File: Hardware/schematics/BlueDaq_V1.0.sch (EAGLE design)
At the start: 67 parts, among them IC1 MEGA8-AI, Q1 MMBT2222, Q2 MMBT2222, Q3 MMBT2222, Q4 MMBT2222, U1 MCP73831, U2 TPS61200, U3 BME280, U4 MIC5225-3.3, U5 MIC5219 5V, X1 USB-MICROB, X2 3.5mm, X4 3.5mm, Y1 16 mhz

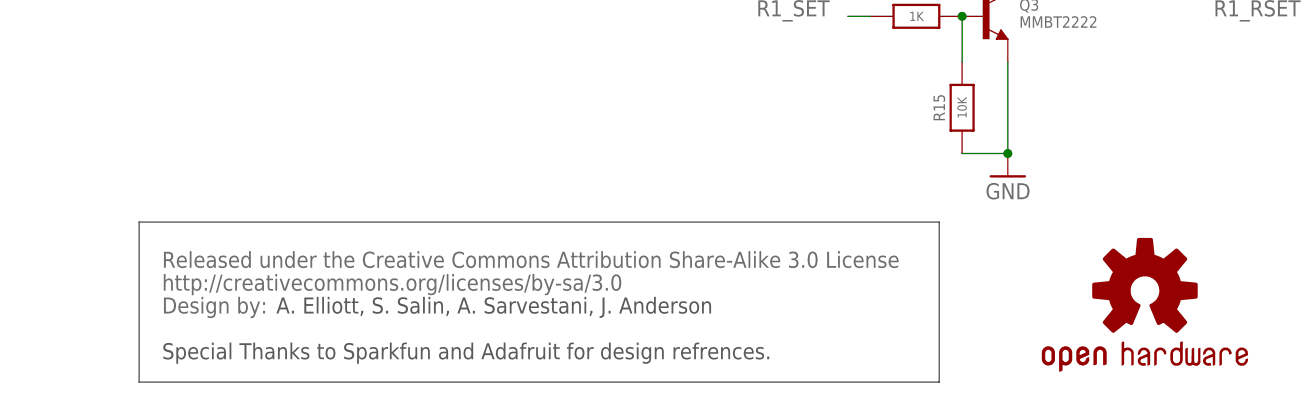
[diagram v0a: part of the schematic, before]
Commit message: moved some stuff to other side of board
starting to make big things on top small stuff on bottom for oven
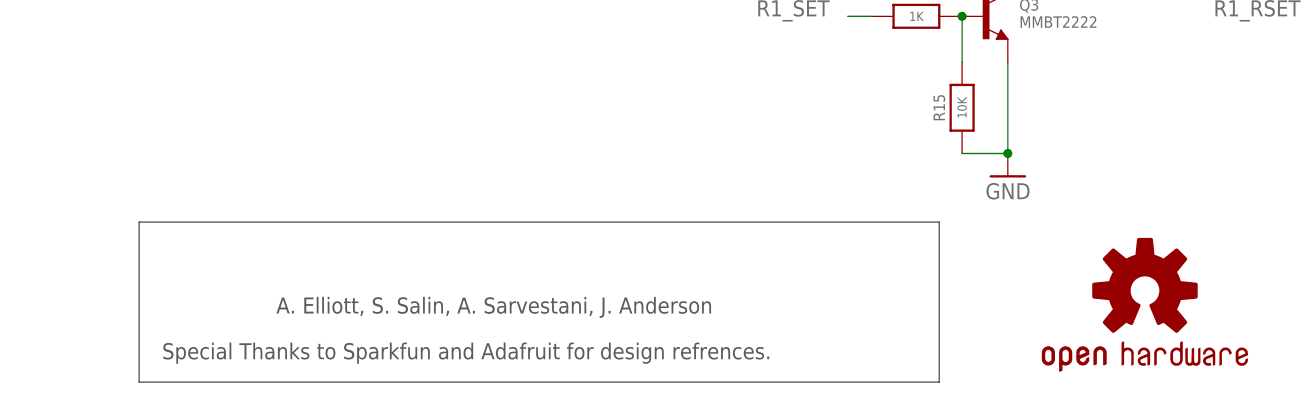
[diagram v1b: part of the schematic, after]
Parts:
- removed U$23: CREATIVE_COMMONS, SparkFun-Aesthetics:CREATIVE_COMMONS
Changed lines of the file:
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@@
 <part name="U$21" library="microbuilder" deviceset="GND" device=""/>
 <part name="U$22" library="SparkFun" deviceset="OSHW-LOGO" device="S"/>
-<part name="U$23" library="SparkFun-Aesthetics" deviceset="CREATIVE_COMMONS" device=""/>
 </parts>
 <sheets>
@@
 <instance part="U$21" gate="G$1" x="81.28" y="218.44"/>
 <instance part="U$22" gate="G$1" x="302.26" y="15.24"/>
-<instance part="U$23" gate="G$1" x="193.04" y="12.7"/>
 </instances>
 <busses>

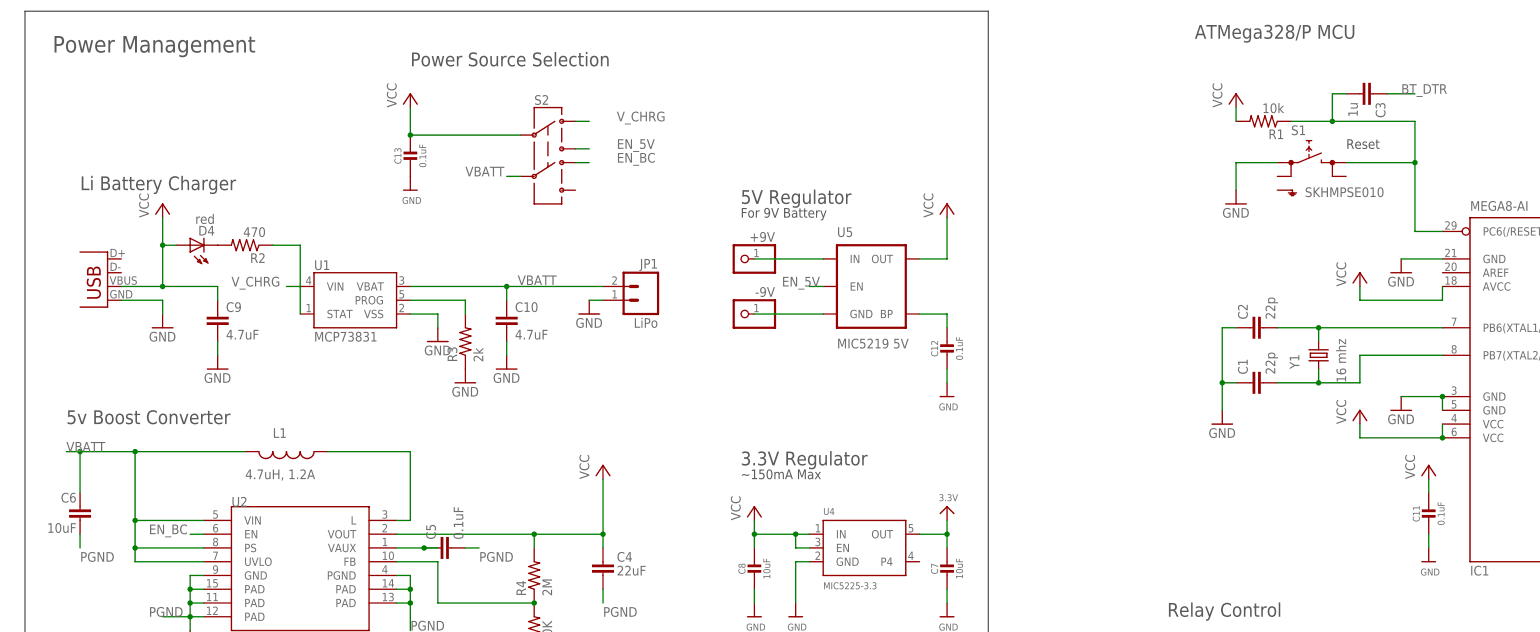
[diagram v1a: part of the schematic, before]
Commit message: updated board
updated layout. starting to have issue connecting gnd properly. added DRU/cam processor for OSH
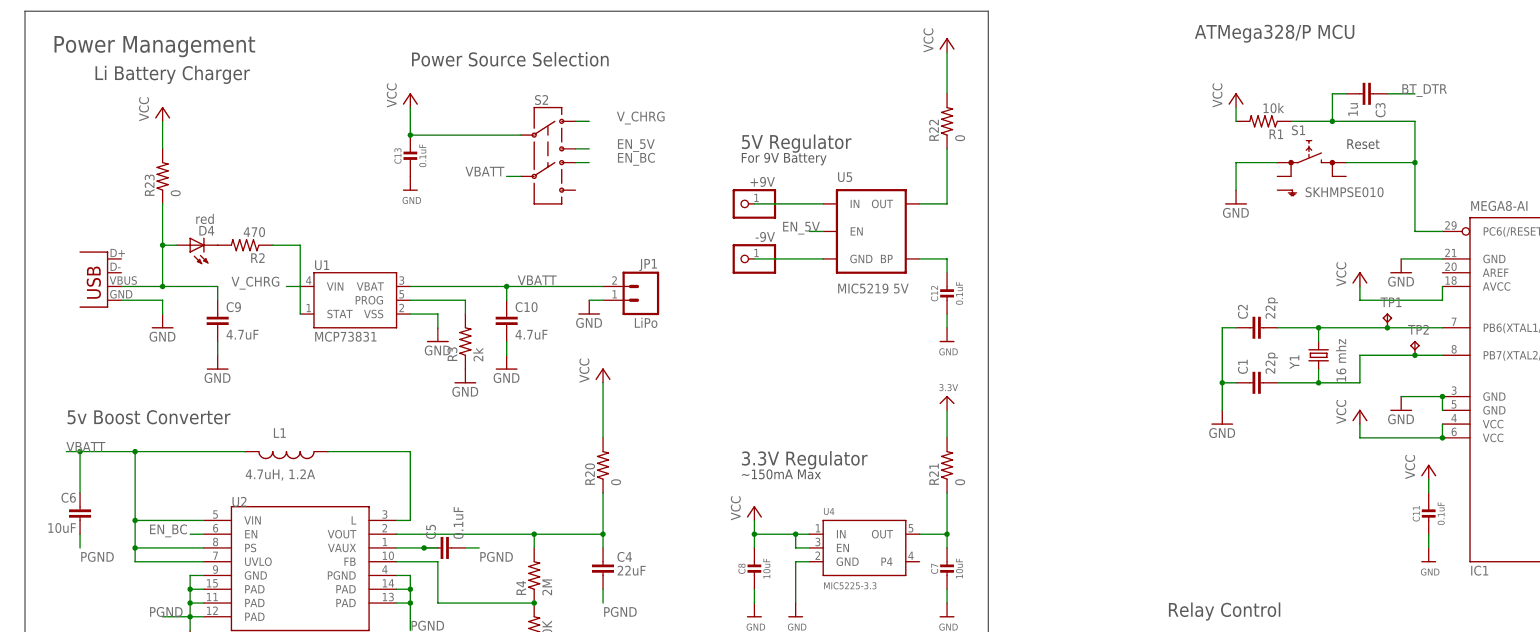
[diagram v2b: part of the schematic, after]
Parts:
- added R20, R21, R22, R23: 0, adafruit:R-US_R0805
- added TP1, TP2: TPTP19SQ, testpad:TPTP19SQ
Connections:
- new net N$20: C4.1, R20.1, R4.2, U2.VOUT
- new net N$21: R22.1, U5.OUT
- new net N$23: C9.1, D4.A, R23.1, X1.VBUS
- new net OUT: C7.1, R21.1, U4.OUT
- net 3.3V: now also R21.2; no longer C7.1, U4.OUT
- net VCC: now also R20.2, R22.2, R23.2; no longer C4.1, C9.1, D4.A, R4.2, U2.VOUT, U5.OUT, X1.VBUS
- net XTAL1: now also TP1.TP
- net XTAL2: now also TP2.TP
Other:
- moved on the sheet: +9V, -9V, C12, U5

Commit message: + Updated Schematic
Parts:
- removed BLUETOOTH: (no value), pinhead:PINHD-1X7
- removed C3: 1u, rcl:C-EUC0603
- removed R6: 10K, adafruit:R-US_R0805
- added C14: 0.1uF, microbuilder:CAP_CERAMIC0805-NOOUTLINE
- added JP2: (no value), adafruit:PINHD-1X6
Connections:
- removed net BT_DSR: BLUETOOTH.3, IC1.PD2(INT0)
- removed net BT_DTR: BLUETOOTH.7, C3.1
- removed net N$5: R6.2, U3.SDO
- new net BT_BRK: IC1.PD2(INT0), JP2.1
- net 3.3V: no longer R6.1
- net BT_RX: now also JP2.2; no longer BLUETOOTH.6
- net BT_STS: now also JP2.5, JP2.6; no longer BLUETOOTH.1
- net BT_TX: now also JP2.3; no longer BLUETOOTH.5
- net GND: now also C11.1, C14.1, JP2.4, U3.SDO; no longer BLUETOOTH.2, C11.2
- net RESET_PIN: no longer C3.2
- net VCC: now also C11.2, C14.2; no longer BLUETOOTH.4, C11.1
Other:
- moved on the sheet: C11

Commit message: + orginization chages
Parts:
- removed JP2: (no value), adafruit:PINHD-1X6
- added BT: (no value), adafruit:PINHD-1X6
- added D8: (no value), adafruit:DIODESMA
- C12: value 0.1uF -> 10uF
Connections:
- removed net N$21: R22.1, U5.OUT
- new net N$18: D8.C, R22.1
- new net N$5: D8.A, U5.OUT
- net BT_BRK: now also BT.1; no longer JP2.1
- net BT_RX: now also BT.2; no longer JP2.2
- net BT_STS: now also BT.6; no longer JP2.5, JP2.6
- net BT_TX: now also BT.3; no longer JP2.3
- net GND: now also BT.4, C4.2, C5.2, C6.2, R5.1, U2.PAD@4, U2.PAD@5, U2.PGND; no longer JP2.4
- net PGND: no longer C4.2, C5.2, C6.2, R5.1, U2.PAD@4, U2.PAD@5, U2.PGND
- net VCC: now also BT.5
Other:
- moved on the sheet: C11, C14, R1, R22

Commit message: Add files via upload
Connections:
- net N$20 renamed VOUT
- removed net PGND: U2.GND, U2.PAD@1, U2.PAD@2, U2.PAD@3
- net GND: now also U2.GND, U2.PAD@1, U2.PAD@2, U2.PAD@3
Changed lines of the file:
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@@
 <?xml version="1.0" encoding="utf-8"?>
 <!DOCTYPE eagle SYSTEM "eagle.dtd">
-<eagle version="7.7.0">
+<eagle version="7.6.0">
 <drawing>
 <settings>
@@
 <layer number="91" name="Nets" color="2" fill="1" visible="yes" active="yes"/>
 <layer number="92" name="Busses" color="1" fill="1" visible="yes" active="yes"/>
-<layer number="93" name="Pins" color="2" fill="1" visible="yes" active="yes"/>
+<layer number="93" name="Pins" color="2" fill="1" visible="no" active="yes"/>
 <layer number="94" name="Symbols" color="4" fill="1" visible="yes" active="yes"/>
 <layer number="95" name="Names" color="7" fill="1" visible="yes" active="yes"/>
@@
 <part name="C5" library="SparkFun" deviceset="CAP" device="0402-CAP" value="0.1uF"/>
 <part name="C6" library="CH_passive" deviceset="CAP" device="1206" value="10uF"/>
-<part name="GND4" library="SparkFun" deviceset="GND" device=""/>
 <part name="L1" library="SparkFun" deviceset="INDUCTOR" device="." value="4.7uH, 1.2A"/>
 <part name="P+5" library="supply1" deviceset="VCC" device=""/>
@@
 <part name="GND21" library="SparkFun" deviceset="GND" device=""/>
 <part name="D8" library="adafruit" deviceset="DIODE" device="SMA"/>
+<part name="GND4" library="SparkFun" deviceset="GND" device=""/>
 </parts>
 <sheets>
@@
 <attribute name="VALUE" x="14.224" y="155.194" size="1.778" layer="96"/>
 </instance>
-<instance part="GND4" gate="1" x="40.64" y="134.62"/>
 <instance part="L1" gate="G$1" x="58.42" y="170.18" smashed="yes" rot="R270">
 <attribute name="NAME" x="55.88" y="172.72" size="1.778" layer="95"/>
@@
 <instance part="GND21" gate="1" x="20.32" y="152.4"/>
 <instance part="D8" gate="G$1" x="180.34" y="223.52" rot="R90"/>
+<instance part="GND4" gate="1" x="40.64" y="134.62"/>
 </instances>
 <busses>
@@
 <pinref part="C6" gate="G$1" pin="2"/>
 <pinref part="GND21" gate="1" pin="GND"/>
+</segment>
+<segment>
+<wire x1="43.18" y1="144.78" x2="40.64" y2="144.78" width="0.1524" layer="91"/>
+<wire x1="40.64" y1="144.78" x2="40.64" y2="142.24" width="0.1524" layer="91"/>
+<wire x1="43.18" y1="142.24" x2="40.64" y2="142.24" width="0.1524" layer="91"/>
+<wire x1="40.64" y1="142.24" x2="40.64" y2="139.7" width="0.1524" layer="91"/>
+<wire x1="43.18" y1="139.7" x2="40.64" y2="139.7" width="0.1524" layer="91"/>
+<wire x1="40.64" y1="139.7" x2="40.64" y2="137.16" width="0.1524" layer="91"/>
+<junction x="40.64" y="142.24"/>
+<junction x="40.64" y="139.7"/>
+<pinref part="U2" gate="G$1" pin="PAD@1"/>
+<pinref part="U2" gate="G$1" pin="PAD@2"/>
+<pinref part="U2" gate="G$1" pin="PAD@3"/>
+<pinref part="U2" gate="G$1" pin="GND"/>
+<wire x1="43.18" y1="147.32" x2="40.64" y2="147.32" width="0.1524" layer="91"/>
+<wire x1="40.64" y1="147.32" x2="40.64" y2="144.78" width="0.1524" layer="91"/>
+<junction x="40.64" y="144.78"/>
+<pinref part="GND4" gate="1" pin="GND"/>
 </segment>
 </net>
@@
 </segment>
 </net>
-<net name="PGND" class="0">
-<segment>
-<wire x1="43.18" y1="144.78" x2="40.64" y2="144.78" width="0.1524" layer="91"/>
-<wire x1="40.64" y1="144.78" x2="40.64" y2="142.24" width="0.1524" layer="91"/>
-<wire x1="43.18" y1="142.24" x2="40.64" y2="142.24" width="0.1524" layer="91"/>
-<wire x1="40.64" y1="142.24" x2="40.64" y2="139.7" width="0.1524" layer="91"/>
-<wire x1="43.18" y1="139.7" x2="40.64" y2="139.7" width="0.1524" layer="91"/>
-<wire x1="40.64" y1="139.7" x2="40.64" y2="137.16" width="0.1524" layer="91"/>
-<junction x="40.64" y="142.24"/>
-<junction x="40.64" y="139.7"/>
-<pinref part="U2" gate="G$1" pin="PAD@1"/>
-<pinref part="U2" gate="G$1" pin="PAD@2"/>
-<pinref part="U2" gate="G$1" pin="PAD@3"/>
-<pinref part="GND4" gate="1" pin="GND"/>
-<pinref part="U2" gate="G$1" pin="GND"/>
-<wire x1="43.18" y1="147.32" x2="40.64" y2="147.32" width="0.1524" layer="91"/>
-<wire x1="40.64" y1="147.32" x2="40.64" y2="144.78" width="0.1524" layer="91"/>
-<junction x="40.64" y="144.78"/>
-</segment>
-</net>
 <net name="R0_SET" class="0">
 <segment>
@@
 </segment>
 </net>
-<net name="N$20" class="0">
+<net name="VOUT" class="0">
 <segment>
 <pinref part="U2" gate="G$1" pin="VOUT"/>

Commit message: lots of changes
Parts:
- removed S2: (no value), SparkFun-Electromechanical:SWITCH-DPDTEG2211
- added C15: 10uF, microbuilder:CAP_CERAMIC0805-NOOUTLINE
- added C3: 0.1uF, microbuilder:CAP_CERAMIC0805-NOOUTLINE
- added D10: (no value), adafruit:DIODESMA
- added R6: 4.7k, adafruit:R-US_R0805
- C12: value 10uF -> .1uF
- C13: value 0.1uF -> 10uF
- R23: value 0 -> 4.7k
- R4: value 2M -> 1.7M
- R5: value 220K -> 180K
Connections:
- removed net EN_5V: S2.3, U5.EN
- removed net EN_BC: S2.4, U2.EN
- removed net V_CHRG: S2.1, U1.VIN
- new net N$20: D10.A, R20.2
- new net N$36: C11.2, IC1.AREF
- net 3.3V: now also R23.2, R6.2
- net GND: now also C15.2, C3.1; no longer C13.2
- net N$15: now also C13.1, U5.EN
- net N$16: now also C13.2
- net N$23: now also U1.VIN; no longer R23.1
- net N$5: now also C15.1
- net SCL: now also R6.1
- net SDA: now also R23.1
- net VBATT: now also U2.EN; no longer S2.5
- net VCC: now also C3.2, D10.C; no longer C11.2, C13.1, R20.2, R23.2, S2.2
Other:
- note added: "ISP"
- note removed: "GND and PGND joined here (datasheet)"
- note removed: "JTAG"
- moved on the sheet: +9V, -9V, C11, C13, R23

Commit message: oh no fix
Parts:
- C1, C2: device rcl:C-EUC0603 -> rcl:C-EUC0805
- C10, C5, C9: device SparkFun:CAP0402-CAP -> SparkFun:CAP0805
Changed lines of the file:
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@@
 <grid distance="0.1" unitdist="inch" unit="inch" style="lines" multiple="1" display="no" altdistance="0.01" altunitdist="inch" altunit="inch"/>
 <layers>
-<layer number="1" name="Top" color="4" fill="1" visible="no" active="no"/>
-<layer number="16" name="Bottom" color="1" fill="1" visible="no" active="no"/>
-<layer number="17" name="Pads" color="2" fill="1" visible="no" active="no"/>
-<layer number="18" name="Vias" color="2" fill="1" visible="no" active="no"/>
-<layer number="19" name="Unrouted" color="6" fill="1" visible="no" active="no"/>
-<layer number="20" name="Dimension" color="15" fill="1" visible="no" active="no"/>
-<layer number="21" name="tPlace" color="7" fill="1" visible="no" active="no"/>
-<layer number="22" name="bPlace" color="7" fill="1" visible="no" active="no"/>
-<layer number="23" name="tOrigins" color="15" fill="1" visible="no" active="no"/>
-<layer number="24" name="bOrigins" color="15" fill="1" visible="no" active="no"/>
-<layer number="25" name="tNames" color="7" fill="1" visible="no" active="no"/>
-<layer number="26" name="bNames" color="7" fill="1" visible="no" active="no"/>
-<layer number="27" name="tValues" color="7" fill="1" visible="no" active="no"/>
-<layer number="28" name="bValues" color="7" fill="1" visible="no" active="no"/>
+<layer number="1" name="Top" color="4" fill="1" visible="yes" active="no"/>
+<layer number="16" name="Bottom" color="1" fill="1" visible="yes" active="no"/>
+<layer number="17" name="Pads" color="2" fill="1" visible="yes" active="no"/>
+<layer number="18" name="Vias" color="2" fill="1" visible="yes" active="no"/>
+<layer number="19" name="Unrouted" color="6" fill="1" visible="yes" active="no"/>
+<layer number="20" name="Dimension" color="15" fill="1" visible="yes" active="no"/>
+<layer number="21" name="tPlace" color="7" fill="1" visible="yes" active="no"/>
+<layer number="22" name="bPlace" color="7" fill="1" visible="yes" active="no"/>
+<layer number="23" name="tOrigins" color="15" fill="1" visible="yes" active="no"/>
+<layer number="24" name="bOrigins" color="15" fill="1" visible="yes" active="no"/>
+<layer number="25" name="tNames" color="7" fill="1" visible="yes" active="no"/>
+<layer number="26" name="bNames" color="7" fill="1" visible="yes" active="no"/>
+<layer number="27" name="tValues" color="7" fill="1" visible="yes" active="no"/>
+<layer number="28" name="bValues" color="7" fill="1" visible="yes" active="no"/>
 <layer number="29" name="tStop" color="7" fill="3" visible="no" active="no"/>
 <layer number="30" name="bStop" color="7" fill="6" visible="no" active="no"/>
@@
 <layer number="35" name="tGlue" color="7" fill="4" visible="no" active="no"/>
 <layer number="36" name="bGlue" color="7" fill="5" visible="no" active="no"/>
-<layer number="37" name="tTest" color="7" fill="1" visible="no" active="no"/>
-<layer number="38" name="bTest" color="7" fill="1" visible="no" active="no"/>
+<layer number="37" name="tTest" color="7" fill="1" visible="yes" active="no"/>
+<layer number="38" name="bTest" color="7" fill="1" visible="yes" active="no"/>
 <layer number="39" name="tKeepout" color="4" fill="11" visible="no" active="no"/>
 <layer number="40" name="bKeepout" color="1" fill="11" visible="no" active="no"/>
@@
 <layer number="44" name="Drills" color="7" fill="1" visible="no" active="no"/>
 <layer number="45" name="Holes" color="7" fill="1" visible="no" active="no"/>
-<layer number="46" name="Milling" color="3" fill="1" visible="no" active="no"/>
-<layer number="47" name="Measures" color="7" fill="1" visible="no" active="no"/>
-<layer number="48" name="Document" color="7" fill="1" visible="no" active="no"/>
-<layer number="49" name="Reference" color="7" fill="1" visible="no" active="no"/>
-<layer number="50" name="dxf" color="7" fill="1" visible="no" active="no"/>
-<layer number="51" name="tDocu" color="6" fill="9" visible="no" active="no"/>
-<layer number="52" name="bDocu" color="7" fill="1" visible="no" active="no"/>
-<layer number="53" name="tGND_GNDA" color="7" fill="9" visible="no" active="no"/>
-<layer number="54" name="bGND_GNDA" color="1" fill="9" visible="no" active="no"/>
-<layer number="56" name="wert" color="7" fill="1" visible="no" active="no"/>
-<layer number="57" name="tCAD" color="7" fill="1" visible="no" active="no"/>
-<layer number="59" name="tCarbon" color="7" fill="1" visible="no" active="no"/>
-<layer number="60" name="bCarbon" color="7" fill="1" visible="no" active="no"/>
+<layer number="46" name="Milling" color="3" fill="1" visible="yes" active="no"/>
+<layer number="47" name="Measures" color="7" fill="1" visible="yes" active="no"/>
+<layer number="48" name="Document" color="7" fill="1" visible="yes" active="no"/>
+<layer number="49" name="Reference" color="7" fill="1" visible="yes" active="no"/>
+<layer number="50" name="dxf" color="7" fill="1" visible="yes" active="no"/>
+<layer number="51" name="tDocu" color="7" fill="1" visible="yes" active="no"/>
+<layer number="52" name="bDocu" color="7" fill="1" visible="yes" active="no"/>
+<layer number="53" name="tGND_GNDA" color="7" fill="9" visible="yes" active="no"/>
+<layer number="54" name="bGND_GNDA" color="1" fill="9" visible="yes" active="no"/>
+<layer number="56" name="wert" color="7" fill="1" visible="yes" active="no"/>
+<layer number="57" name="tCAD" color="7" fill="1" visible="yes" active="no"/>
+<layer number="59" name="tCarbon" color="7" fill="1" visible="yes" active="no"/>
+<layer number="60" name="bCarbon" color="7" fill="1" visible="yes" active="no"/>
 <layer number="90" name="Modules" color="5" fill="1" visible="yes" active="yes"/>
 <layer number="91" name="Nets" color="2" fill="1" visible="yes" active="yes"/>
@@
 <part name="P+1" library="supply1" deviceset="VCC" device=""/>
 <part name="FRAME1" library="frames" deviceset="A3L-LOC" device=""/>
-<part name="C1" library="rcl" deviceset="C-EU" device="C0603" value="22p"/>
-<part name="C2" library="rcl" deviceset="C-EU" device="C0603" value="22p"/>
+<part name="C1" library="rcl" deviceset="C-EU" device="C0805" value="22p"/>
+<part name="C2" library="rcl" deviceset="C-EU" device="C0805" value="22p"/>
 <part name="Y1" library="SparkFun-FreqCtrl" deviceset="CRYSTAL" device="HC49UV" value="16 mhz"/>
 <part name="JTAG" library="pinhead" deviceset="PINHD-2X3" device=""/>
@@
 <part name="P+4" library="supply1" deviceset="VCC" device=""/>
 <part name="S1" library="switch" deviceset="SKHMP*E010" device="" technology="S" value="SKHMPSE010"/>
-<part name="C9" library="SparkFun" deviceset="CAP" device="0402-CAP" value="4.7uF"/>
-<part name="C10" library="SparkFun" deviceset="CAP" device="0402-CAP" value="4.7uF"/>
+<part name="C9" library="SparkFun" deviceset="CAP" device="0805" value="4.7uF"/>
+<part name="C10" library="SparkFun" deviceset="CAP" device="0805" value="4.7uF"/>
 <part name="GND18" library="supply1" deviceset="GND" device=""/>
 <part name="GND20" library="supply1" deviceset="GND" device=""/>
@@
 <part name="C4" library="CH_passive" deviceset="CAP" device="0805" value="22uF"/>
 <part name="U2" library="SparkFun" deviceset="TPS61200" device=""/>
-<part name="C5" library="SparkFun" deviceset="CAP" device="0402-CAP" value="0.1uF"/>
+<part name="C5" library="SparkFun" deviceset="CAP" device="0805" value="0.1uF"/>
 <part name="C6" library="CH_passive" deviceset="CAP" device="1206" value="10uF"/>
 <part name="L1" library="SparkFun" deviceset="INDUCTOR" device="." value="4.7uH, 1.2A"/>
